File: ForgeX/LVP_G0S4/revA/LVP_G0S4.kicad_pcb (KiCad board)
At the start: 2 copper layers, 159.9 x 47.5 mm, 65 parts, among them J1 Conn_02x05_Odd_Even, J10 Conn_01x02_Pin, J11 Conn_01x02_Pin, J12 Conn_01x02_Pin, J13 Conn_01x02_Pin, J14 Conn_02x05_Odd_Even, J15 Conn_01x05_Pin, J16 Conn_01x04, J17 Conn_01x04, J2 Conn_02x05_Odd_Even, J3 Conn_02x05_Odd_Even, J4 Conn_02x05_Odd_Even, J6 Conn_02x20_Odd_Even, J7 Conn_01x02_Pin, J8 Conn_01x02_Pin, J9 Screw_Terminal_01x11, Q2 AO3400A, U1 SSIT3490EESA, U2 SSIT3490EESA, U3 SSIT3490EESA, U4 AMS1117-3.3, U5 LM311, U6 LM311, U7 LM311

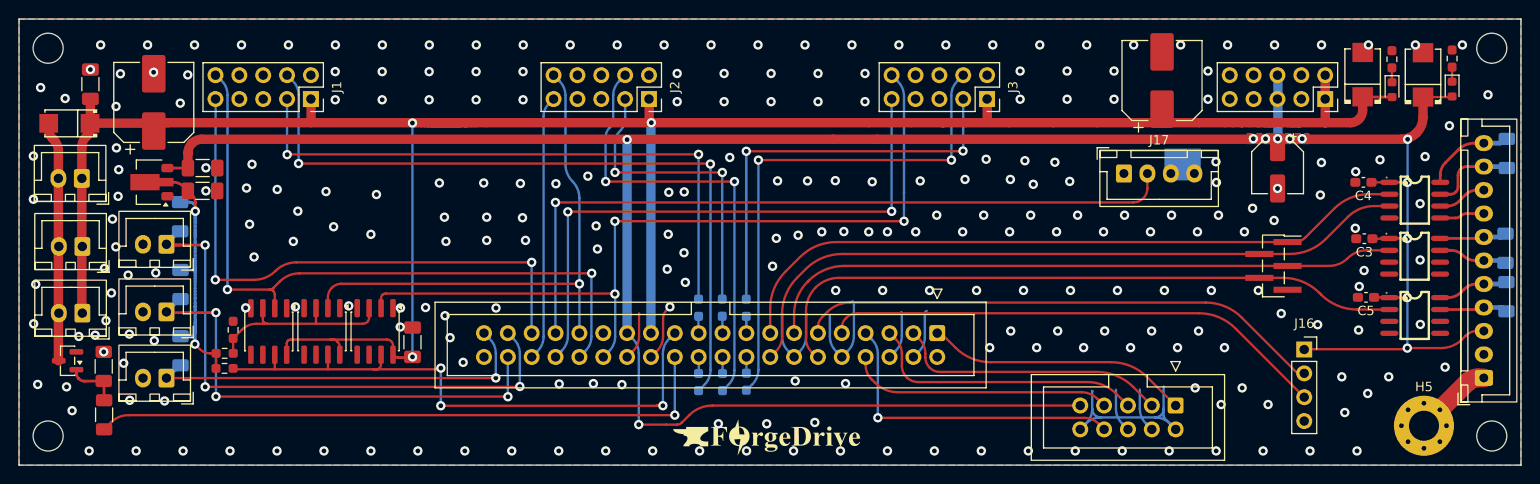
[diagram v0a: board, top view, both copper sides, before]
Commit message: BlackDev Fini & HBM mod
Finalized blackDev, HBM with (RC) ground coupling, LVP swapping RS422 to RS485 and processing card interface modifications
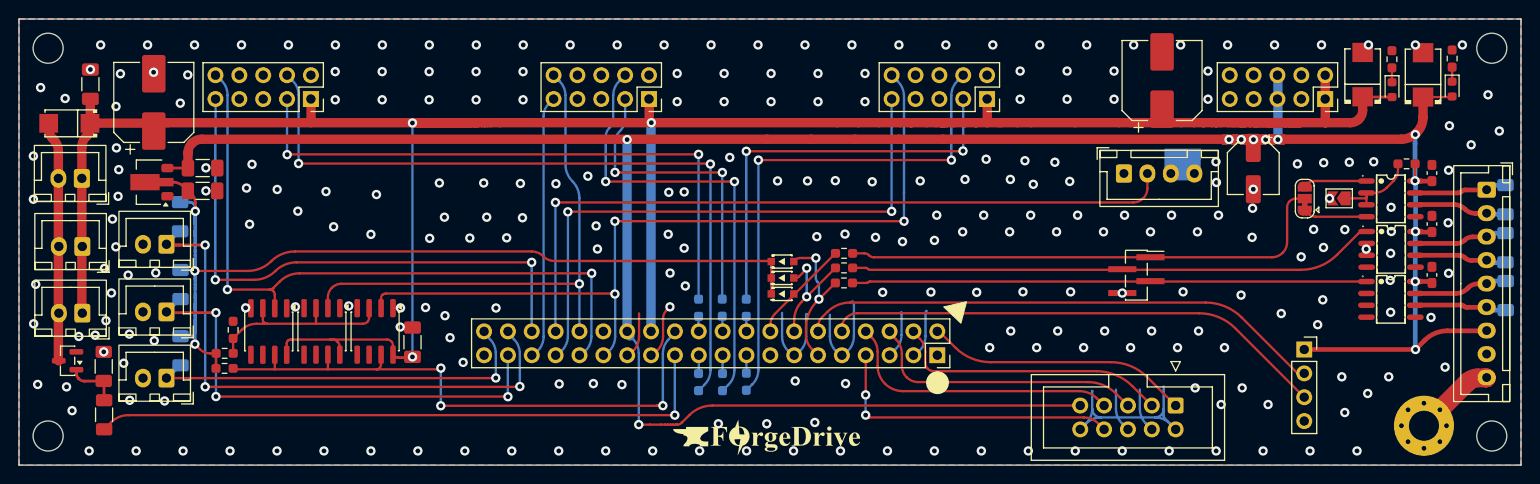
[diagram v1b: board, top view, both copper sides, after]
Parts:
- removed C5: 0.1u, Capacitor_SMD:C_0603_1608Metric_Pad1.08x0.95mm_HandSolder
- removed J15: Conn_01x05_Pin, Connector_PinHeader_1.27mm:PinHeader_1x05_P1.27mm_Vertical_SMD_Pin1Right
- added C11: 0.1u, Capacitor_SMD:C_0603_1608Metric_Pad1.08x0.95mm_HandSolder, F.Cu at (211.3, 80.1)
- added D7: SD103AWS_C5345966, EasyEDA:SOD-323_L1.7-W1.3-LS2.5-RD, F.Cu at (142.2, 85.9)
- added D8: SD103AWS_C5345966, EasyEDA:SOD-323_L1.7-W1.3-LS2.5-RD, F.Cu at (142.2, 84.1)
- added D9: SD103AWS_C5345966, EasyEDA:SOD-323_L1.7-W1.3-LS2.5-RD, F.Cu at (142.2, 87.6)
- added J5: Conn_01x04_Pin, Connector_PinHeader_1.27mm:PinHeader_1x04_P1.27mm_Vertical_SMD_Pin1Right, F.Cu at (179.9, 85.6)
- added JP1: SolderJumper_3_Bridged12, Jumper:SolderJumper-3_P1.3mm_Bridged12_RoundedPad1.0x1.5mm, F.Cu at (197.8, 77.4)
- added JP2: SolderJumper_2_Open, Jumper:SolderJumper-2_P1.3mm_Open_TrianglePad1.0x1.5mm, F.Cu at (201.5, 77.4)
- added R19: 10k, Resistor_SMD:R_0603_1608Metric_Pad0.98x0.95mm_HandSolder, F.Cu at (208.6, 73.7)
- added R20: 220, Resistor_SMD:R_0603_1608Metric_Pad0.98x0.95mm_HandSolder, F.Cu at (148.7, 84.8)
- added R22: 220, Resistor_SMD:R_0603_1608Metric_Pad0.98x0.95mm_HandSolder, F.Cu at (148.7, 86.4)
- added R23: 220, Resistor_SMD:R_0603_1608Metric_Pad0.98x0.95mm_HandSolder, F.Cu at (148.7, 83.3)
- J6: footprint Connector_IDC:IDC-Header_2x20_P2.54mm_Vertical -> Connector_PinSocket_2.54mm:PinSocket_2x20_P2.54mm_Vertical
- J9: value Screw_Terminal_01x11 -> Screw_Terminal_01x09; footprint Connector_JST:JST_XH_B11B-XH-A_1x11_P2.50mm_Vertical -> Connector_JST:JST_XH_B9B-XH-A_1x09_P2.50mm_Vertical
- U1, U2, U3: value SSIT3490EESA -> SP485EEN-TD; footprint EasyEDA:SOIC-8_L5.0-W4.0-P1.27-LS6.0-BL -> EasyEDA:SOIC-8_L4.9-W3.9-P1.27-LS6.0-BL
- moved J9 20.0 mm to (217.2, 76.5), turned to -90 degrees
- moved C3 8.17 mm to (211.3, 85.6), turned to 90 degrees
- moved C4 7.37 mm to (211.3, 74.7), turned to 90 degrees
- moved R12 4.93 mm to (219.2, 77.5), turned to -90 degrees
- moved U3 3.07 mm to (207.0, 88.2)
- moved U2 2.61 mm to (207.0, 82.8)
- moved C8 2.59 mm to (192.3, 74.2)
- moved U1 2.55 mm to (207.0, 77.5)
- moved J6 2.36 mm to (158.7, 94.1)
- moved R15 0.14 mm to (219.2, 87.8), turned to -90 degrees
- moved R14 0.07 mm to (219.2, 82.7), turned to -90 degrees
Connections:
- net /EXP_INT renamed /EXP_CS1
- J6 pad 1: /EXP_SCLK -> GND
- J6 pad 10: GND -> /EXP_TX
- J6 pad 11: /EXP_RX -> /ENC_R3
- J6 pad 12: /ENC_R3 -> /EXP_RX
- J6 pad 13: /ENC_R2 -> GND
- J6 pad 14: GND -> /ENC_R2
- J6 pad 15: /ENC_R1 -> /EXP_CS2
- J6 pad 16: /ENC_T1 -> /ENC_R1
- J6 pad 2: GND -> /EXP_SCLK
- J6 pad 23: /~{BKIN} -> /FAN0
- J6 pad 24: /FAN0 -> /~{BKIN}
- J6 pad 25: +12V -> GND
- J6 pad 26: GND -> +12V
- J6 pad 27: +5V -> GND
- J6 pad 28: GND -> +5V
- J6 pad 29: unconnected-(J6-Pin_29-Pad29) -> /Csense_{A}
- J6 pad 3: /EXP_MOSI -> GND
- J6 pad 30: /Csense_{A} -> unconnected-(J6-Pin_30-Pad30)
- J6 pad 31: /Csense_{B} -> /Csense_{C}
- J6 pad 32: /Csense_{C} -> /Csense_{B}
- J6 pad 33: /HVDC_Cnd -> /Phase_Cnd_{A}
- J6 pad 34: /Phase_Cnd_{A} -> /HVDC_Cnd
- J6 pad 35: /Phase_Cnd_{C} -> /Phase_Cnd_{B}
- J6 pad 36: /Phase_Cnd_{B} -> /Phase_Cnd_{C}
- J6 pad 37: /TEMP1 -> /TEMP2
- J6 pad 38: /TEMP2 -> /TEMP1
- J6 pad 39: /TEMP3 -> GND
- J6 pad 4: GND -> /EXP_MOSI
- J6 pad 40: GND -> /TEMP3
- J6 pad 5: /EXP_MISO -> GND
- J6 pad 6: GND -> /EXP_MISO
- J6 pad 9: /EXP_TX -> GND
- J9 pad 1: Earth -> /ENC_R1-
- J9 pad 2: GND -> /ENC_R1+
- J9 pad 3: +5V -> /ENC_R2-
- J9 pad 4: /ENC_R3- -> /ENC_R2+
- J9 pad 5: /ENC_R3+ -> /ENC_R3-
- J9 pad 6: /ENC_R2- -> /ENC_R3+
- J9 pad 7: /ENC_R2+ -> +5V
- J9 pad 8: /ENC_T1- -> GND
- J9 pad 9: /ENC_T1+ -> Earth
- R1 pad 1: Net-(J6-Pin_17) -> Net-(J6-Pin_18)
- R2 pad 2: Net-(J6-Pin_18) -> Net-(J6-Pin_17)
- R3 pad 1: Net-(J6-Pin_19) -> Net-(J6-Pin_20)
- R4 pad 1: Net-(J6-Pin_21) -> Net-(J6-Pin_22)
- R5 pad 2: Net-(J6-Pin_20) -> Net-(J6-Pin_19)
- R6 pad 2: Net-(J6-Pin_22) -> Net-(J6-Pin_21)
- U1 pad 1: +5V -> Net-(JP1-B)
- U1 pad 2: /ENC_R1 -> Net-(JP2-A)
- U1 pad 3: /ENC_T1 -> Net-(JP2-A)
- U1 pad 4: GND -> Net-(JP1-A)
- U1 pad 5: /ENC_T1- -> GND
- U1 pad 6: /ENC_T1+ -> /ENC_R1+
- U1 pad 8: /ENC_R1+ -> +5V
- U2 pad 1: +5V -> /ENC_R2P
- U2 pad 2: /ENC_R2 -> GND
- U2 pad 3: unconnected-(U2-DI-Pad3) -> GND
- U2 pad 4: GND -> unconnected-(U2-DI-Pad4)
- U2 pad 5: unconnected-(U2-Y-Pad5) -> GND
- U2 pad 6: unconnected-(U2-Z-Pad6) -> /ENC_R2+
- U2 pad 8: /ENC_R2+ -> +5V
- U3 pad 1: +5V -> /ENC_R3P
- U3 pad 2: /ENC_R3 -> GND
- U3 pad 3: unconnected-(U3-DI-Pad3) -> GND
- U3 pad 4: GND -> unconnected-(U3-DI-Pad4)
- U3 pad 5: unconnected-(U3-Y-Pad5) -> GND
- U3 pad 6: unconnected-(U3-Z-Pad6) -> /ENC_R3+
- U3 pad 8: /ENC_R3+ -> +5V
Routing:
- net /ENC_T1: track 74.8 -> 0.00 mm
- net +3.3V: track 29.6 -> 94.9 mm, vias 2 -> 3
- net /ENC_R1: track 74.1 -> 11.1 mm
- net /ENC_R2P: track 0.00 -> 56.2 mm
- net /ENC_R2: track 68.6 -> 13.1 mm, vias 0 -> 2
- net /ENC_R3P: track 0.00 -> 54.8 mm
- net /ENC_R3: track 70.4 -> 16.2 mm, vias 0 -> 2
- net /ENC_R1P: track 0.00 -> 53.4 mm
- net Net-(JP2-A): track 0.00 -> 9.64 mm
- net Net-(JP1-A): track 0.00 -> 6.79 mm
- net Net-(JP1-B): track 0.00 -> 6.78 mm
- net /ENC_T1+: track 5.17 -> 0.00 mm
- net /ENC_T1-: track 4.76 -> 0.00 mm
- net +5V: track 281.3 -> 278.1 mm
- net /EXP_CS0: track 28.2 -> 30.5 mm
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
